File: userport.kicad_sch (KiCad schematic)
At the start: 13 parts, among them J17 C64_Tape_Port, J18 BA60BC0WT, J19 C64_User_Port, U16 74LVC374, U17 74LVC374, U18 74LS374, U19 74LS374, U20 74LS125, U21 74LS125, U23 74LVC374, U24 74LS125, U25 74LS374, U26 74LS374

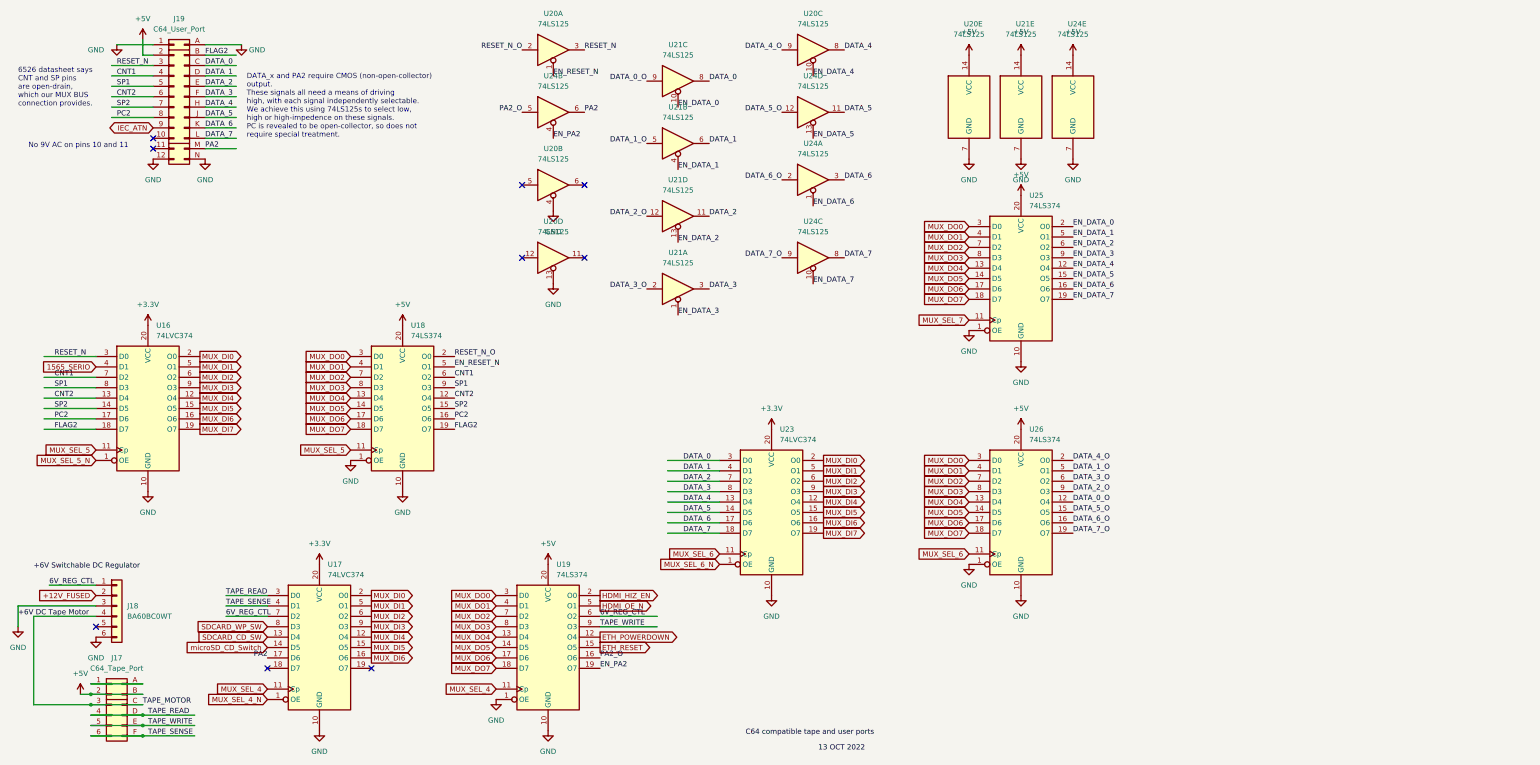
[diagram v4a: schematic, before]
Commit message: rework user port
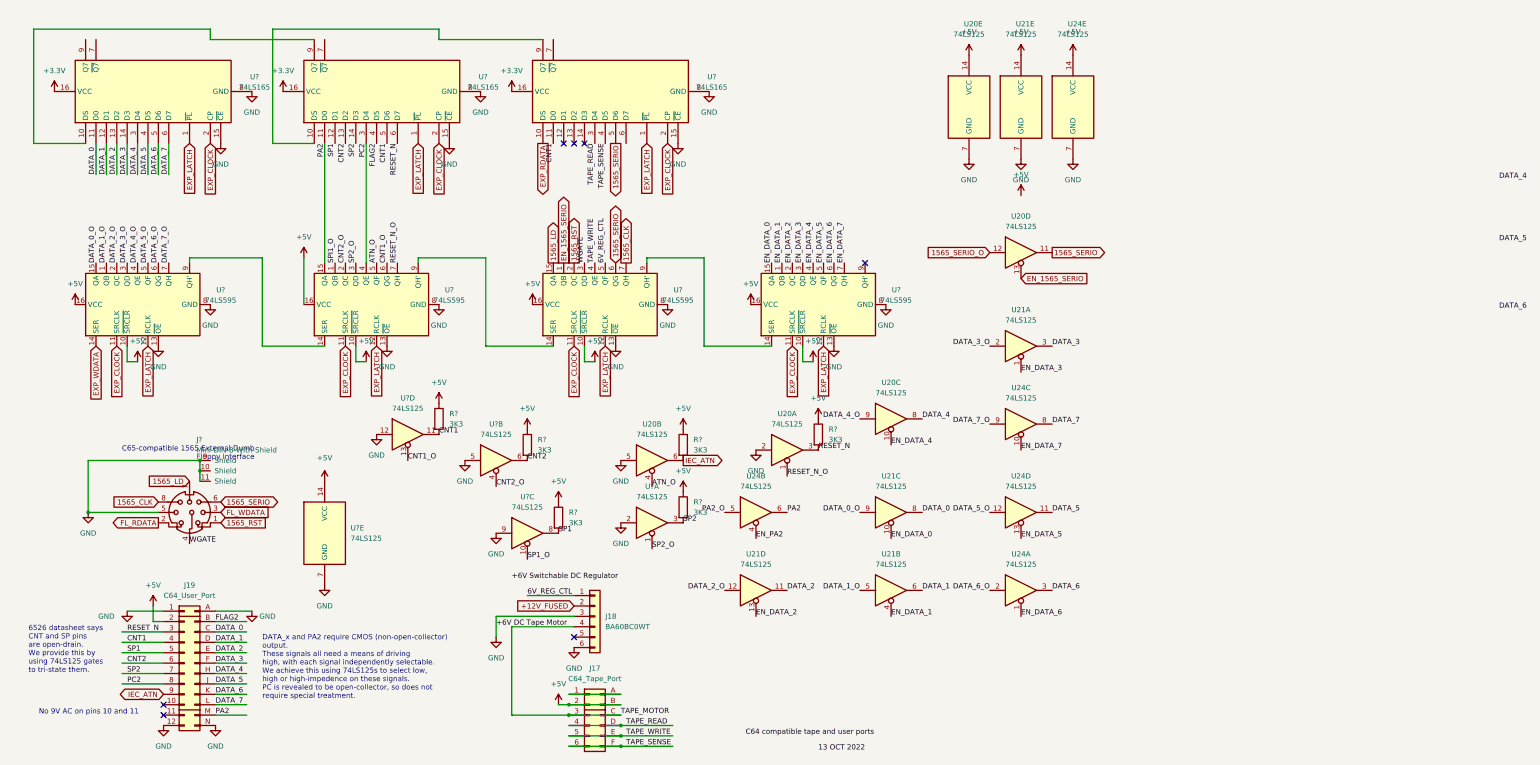
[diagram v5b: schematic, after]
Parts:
- removed U16, U17, U23: 74LVC374, snapeda:DIP-20_LVC_Family, symbol 74xx:74HC374
- removed U18, U19, U25, U26: 74LS374, snapeda:DIP-20_LS_Family, symbol 74xx:74LS374
- added J?: Mini-DIN-8-With-Shield, snapeda:mini-DIN-8, symbol 00Project-SDF-60J:Mini-DIN-8-With-Shield
- added R? (x6): 3K3, snapeda:Labeled Resistor, symbol Device:R
- added U? (x3): 74LS165, snapeda:DIP-16_LVC_Family, symbol 74xx:74LS165
- added U? (x5): 74LS125, symbol 74xx:74LS125
- added U? (x4): 74LS595, snapeda:DIP-16_LS_Family, symbol 74xx:74LS595
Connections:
- net EN_RESET_N is gone; now on net RESET_N_O: U20.1
- net +3V3: now also U?.16 (VCC), U?.16 (VCC), U?.16 (VCC)
- net +5V: now also R?.1, R?.1, R?.1, R?.1, R?.1, R?.1, U?.10 (~{SRCLR}), U?.10 (~{SRCLR}), U?.10 (~{SRCLR}), U?.10 (~{SRCLR}), U?.14 (VCC), U?.16 (VCC), U?.16 (VCC), U?.16 (VCC), U?.16 (VCC)
- net 1565_SERIO: now also U20.11, J?.6, U?.5 (D6), U?.6 (QG)
- net 6V_REG_CTL: now also U?.5 (QF)
- net CNT1: now also R?.2, U?.11, U?.11 (D0), U?.5 (D6)
- net CNT2: now also R?.2, U?.13 (D2), U?.6
- net DATA_0: now also U?.11 (D0)
- net DATA_0_O: now also U?.15 (QA)
- net DATA_1: now also U?.12 (D1)
- net DATA_1_O: now also U?.1 (QB)
- net DATA_2: now also U?.13 (D2)
- net DATA_2_O: now also U?.2 (QC)
- net DATA_3: now also U?.14 (D3)
- net DATA_3_O: now also U?.3 (QD)
- net DATA_4: now also U?.3 (D4)
- net DATA_4_O: now also U?.4 (QE)
- net DATA_5: now also U?.4 (D5)
- net DATA_5_O: now also U?.5 (QF)
- net DATA_6: now also U?.5 (D6)
- net DATA_6_O: now also U?.6 (QG)
- net DATA_7: now also U?.6 (D7)
- net DATA_7_O: now also U?.7 (QH)
- net EN_DATA_0: now also U?.15 (QA)
- net EN_DATA_1: now also U?.1 (QB)
- net EN_DATA_2: now also U?.2 (QC)
- net EN_DATA_3: now also U?.3 (QD)
- net EN_DATA_4: now also U?.4 (QE)
- net EN_DATA_5: now also U?.5 (QF)
- net EN_DATA_6: now also U?.6 (QG)
- net EN_DATA_7: now also U?.7 (QH)
- net FLAG2: now also U?.4 (D5)
- net GND: now also U20.2, U20.5, J?.10 (Shield), J?.11 (Shield), J?.5, J?.9 (Shield), U?.12, U?.13 (~{OE}), U?.13 (~{OE}), U?.13 (~{OE}), U?.13 (~{OE}), U?.15 (~{CE}), U?.15 (~{CE}), U?.15 (~{CE}), U?.2, U?.5, U?.7 (GND), U?.8 (GND), U?.8 (GND), U?.8 (GND), U?.8 (GND), U?.8 (GND), U?.8 (GND), U?.8 (GND), U?.9; no longer U20.13, U20.4
- net IEC_ATN: now also U20.6, R?.2
- net PA2: now also U?.11 (D0), U?.15 (QA)
- net PC2: now also U?.3 (D4), U?.4 (QE)
- net RESET_N: now also R?.2, U?.6 (D7)
- net RESET_N_O: now also U?.7 (QH); no longer U20.2
- net SP1: now also R?.2, U?.12 (D1), U?.8
- net SP2: now also R?.2, U?.14 (D3), U?.3
- net TAPE_READ: now also U?.3 (D4)
- net TAPE_SENSE: now also U?.4 (D5)
- net TAPE_WRITE: now also U?.4 (QE)
- net 1565_SERIO_O: now reaches U20.12
- new net: U?.10 (DS), U?.9 (Q7) (x2)
- new net: U?.14 (SER), U?.9 (QH') (x3)
- new net 1565_CLK: J?.8, U?.7 (QH)
- new net 1565_LD: J?.7, U?.15 (QA)
- new net 1565_RST: J?.1, U?.2 (QC)
- new net ATN_O: U20.4, U?.5 (QF)
- new net CNT1_O: U?.13, U?.6 (QG)
- new net CNT2_O: U?.2 (QC), U?.4
- new net EN_1565_SERIO: U20.13, U?.1 (QB)
- new net EXP_CLOCK: U?.11 (SRCLK), U?.11 (SRCLK), U?.11 (SRCLK), U?.11 (SRCLK), U?.2 (CP), U?.2 (CP), U?.2 (CP)
- new net EXP_LATCH: U?.1 (~{PL}), U?.1 (~{PL}), U?.1 (~{PL}), U?.12 (RCLK), U?.12 (RCLK), U?.12 (RCLK), U?.12 (RCLK)
- new net EXP_RDATA: U?.10 (DS)
- new net EXP_WDATA: U?.14 (SER)
- new net FL_RDATA: J?.2
- new net FL_WDATA: J?.3
- new net SP1_O: U?.10
- new net SP2_O: U?.1, U?.3 (QD)
- new net SPI1_O: U?.1 (QB)
- new net WGATE: J?.4, U?.3 (QD)
- no-connect marks 9 -> 7
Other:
- note added: "6526 datasheet says CNT and SP pins are open-drain. We provide this by using 74LS125 gates to tri-state them."
- note added: "C65-compatible 1565 External Dumb Floppy Interface"
- note removed: "6526 datasheet says CNT and SP pins are open-drain, which our MUX BUS connection provides."
- moved on the sheet: J17, J18, J19, U20A, U20B, U20C, U20D, U21A, U21B, U21C, U21D, U24A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

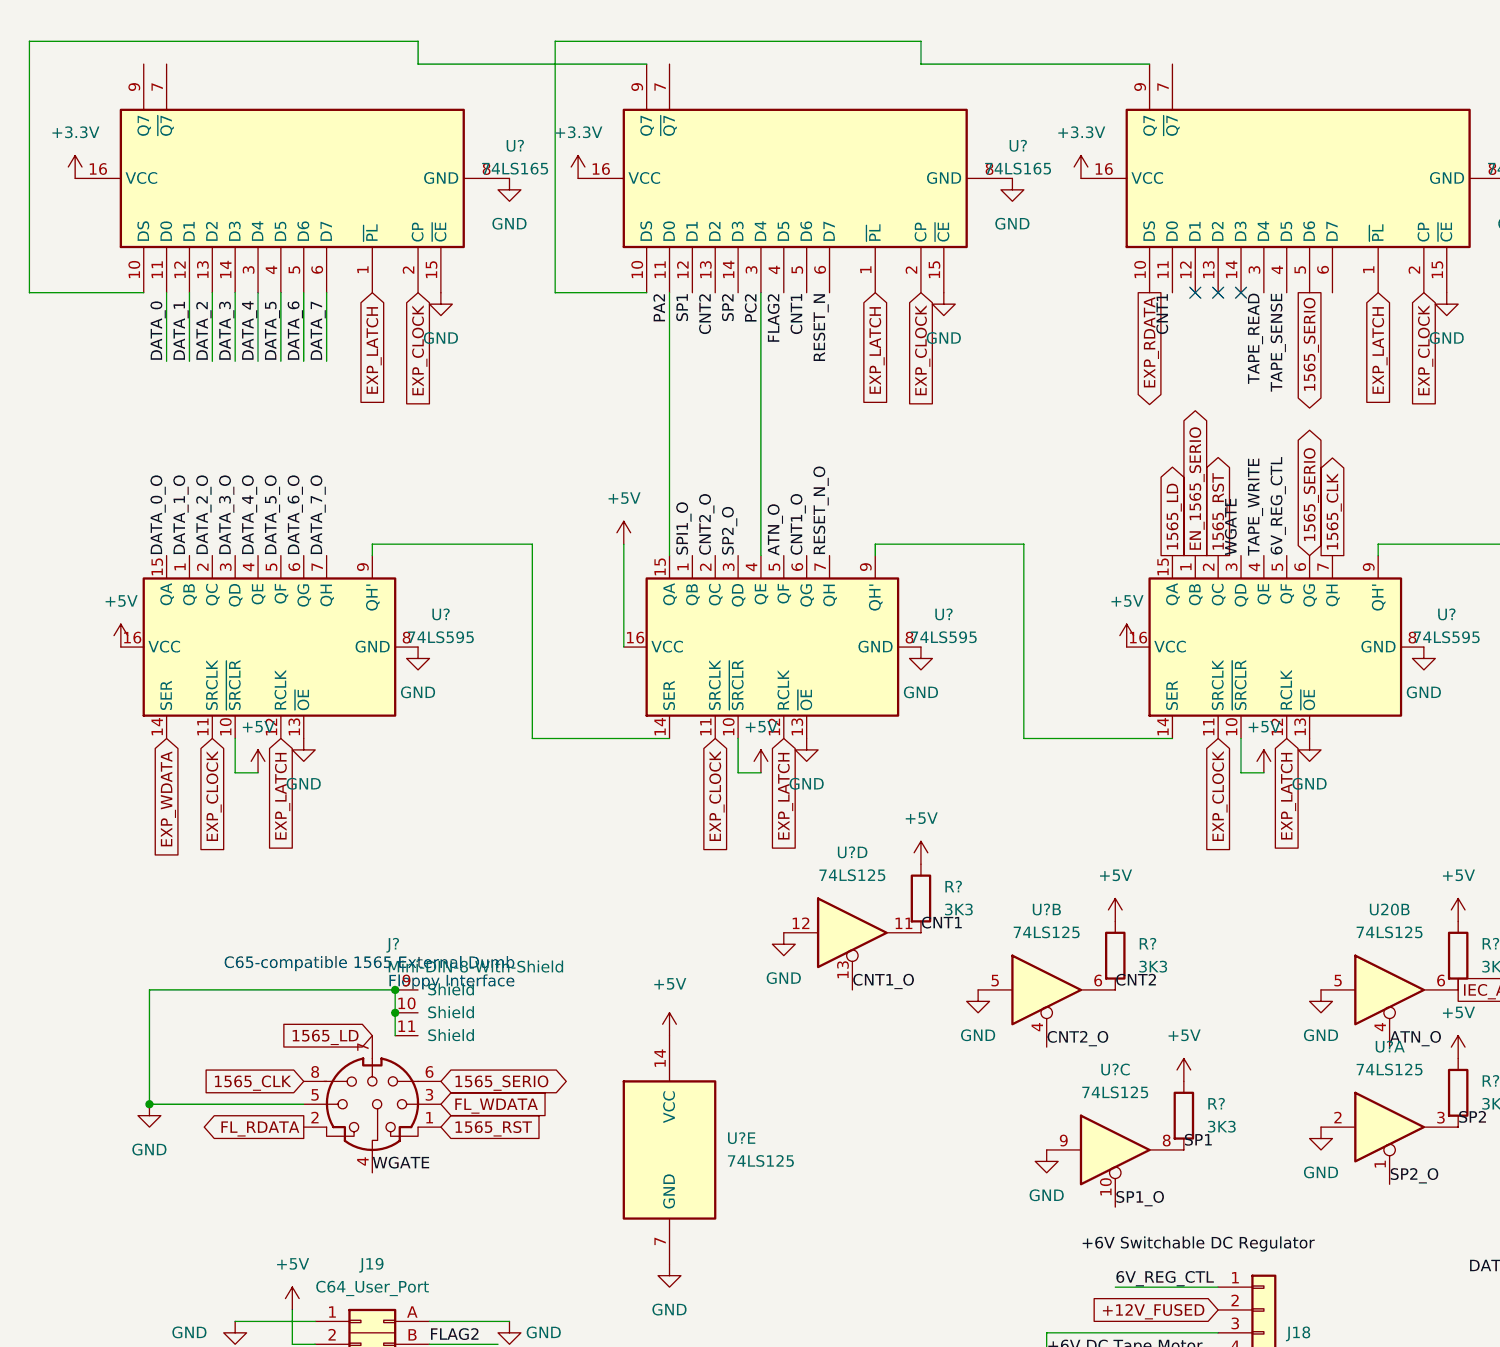
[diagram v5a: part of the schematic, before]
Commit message: reconnect everything and add PMOD and 34pin floppy connectors
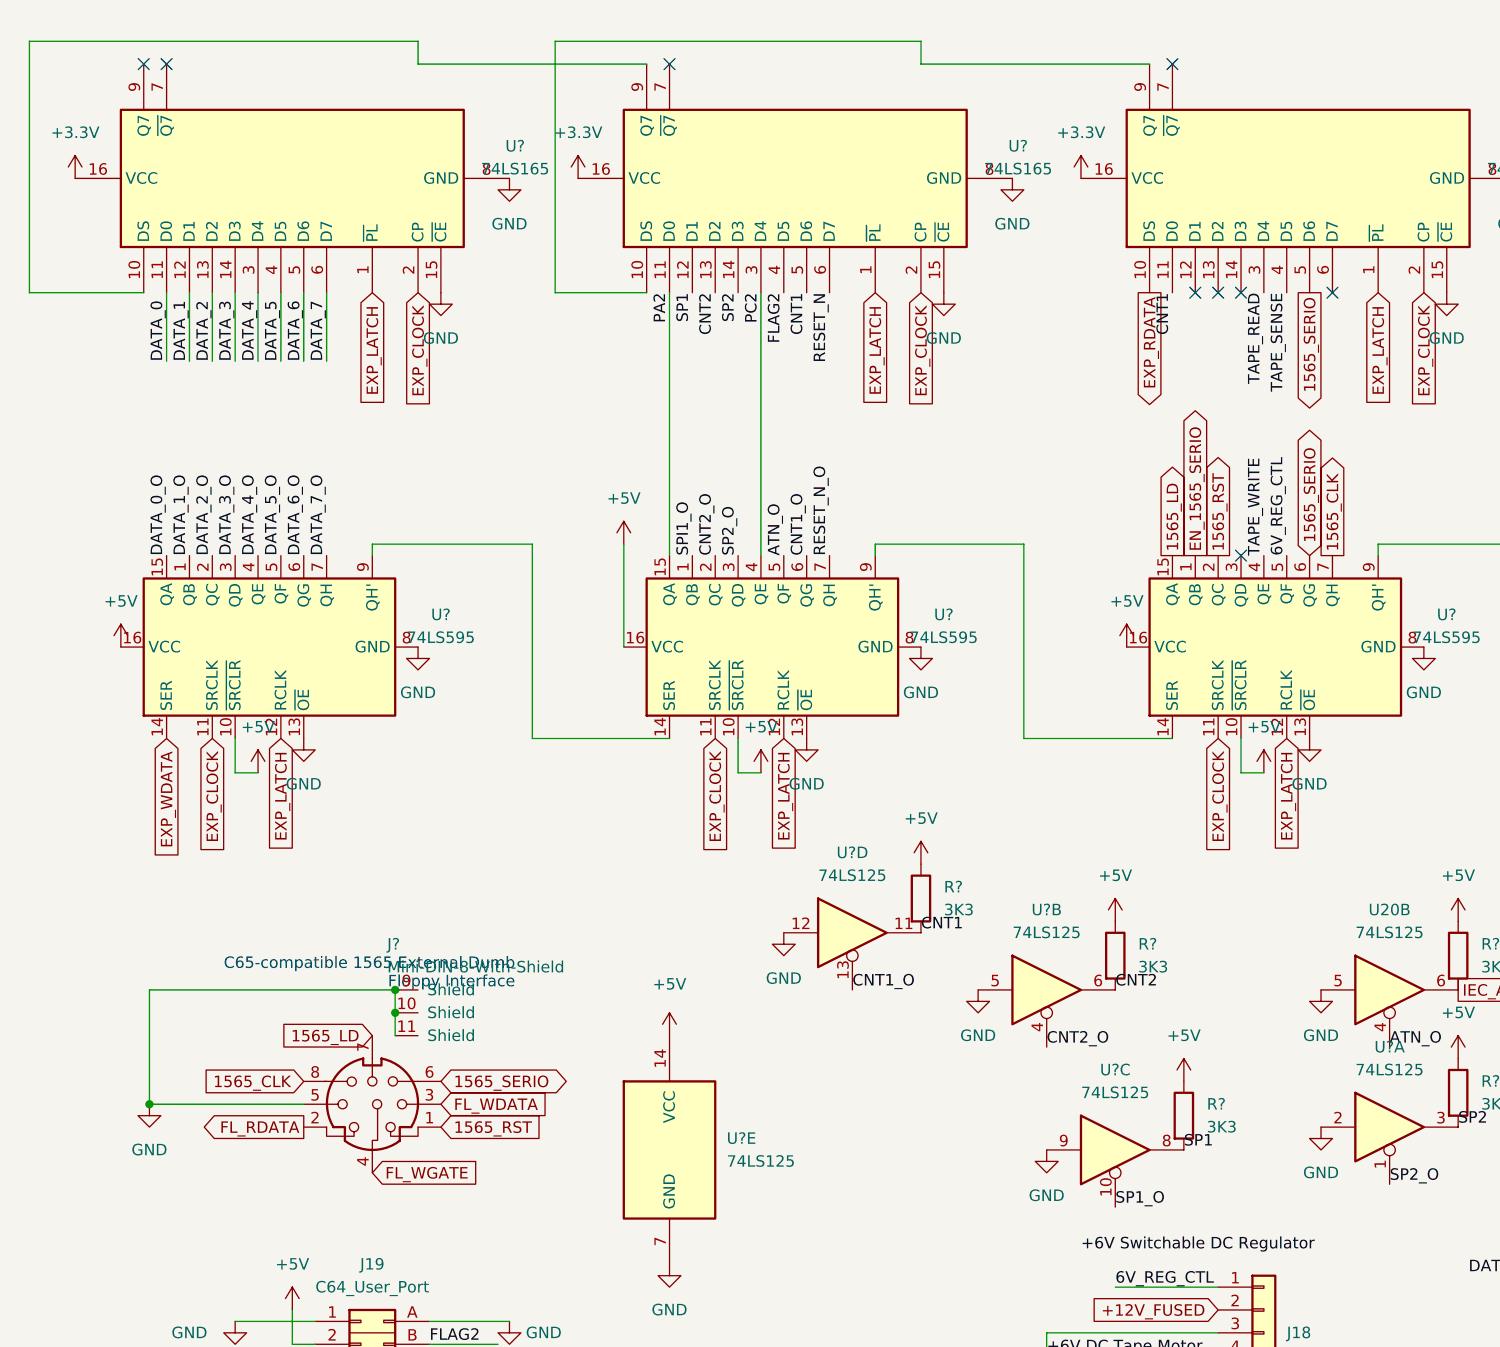
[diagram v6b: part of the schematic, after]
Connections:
- net WGATE: no longer names the net of U?.3 (QD)
- net WGATE: no longer J?.4
- new net FL_WGATE: J?.4
- no-connect marks 7 -> 13
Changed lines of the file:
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@@
   (junction (at 148.59 182.88) (diameter 0) (color 0 0 0 0)
   )
+  (no_connect (at 162.56 45.72))
+  (no_connect (at 88.9 20.32))
+  (no_connect (at 144.78 20.32))
+  (no_connect (at 30.48 20.32))
+  (no_connect (at 33.02 20.32))
   (no_connect (at 149.86 45.72))
   (no_connect (at 152.4 45.72))
   (no_connect (at 147.32 45.72))
+  (no_connect (at 152.4 74.93))
   (no_connect (at 49.53 182.88))
   (no_connect (at 149.86 166.37))
@@
     (effects (font (size 1.27 1.27)) (justify left bottom))
   )
-  (label "WGATE" (at 55.88 143.51 0)
-    (effects (font (size 1.27 1.27)) (justify left bottom))
-  )
   (label "DATA_0_O" (at 219.71 135.89 180)
     (effects (font (size 1.27 1.27)) (justify right bottom))
@@
   )
   (label "SP2" (at 176.53 138.43 0)
-    (effects (font (size 1.27 1.27)) (justify left bottom))
-  )
-  (label "WGATE" (at 152.4 74.93 90)
     (effects (font (size 1.27 1.27)) (justify left bottom))
   )
@@
     )
   )
+  (global_label "FL_WGATE" (shape input) (at 55.88 143.51 0) (fields_autoplaced)
+    (effects (font (size 1.27 1.27)) (justify left))
+    (property "Intersheet References" "${INTERSHEET_REFS}" (id 0) (at 67.2152 143.4306 0)
+      (effects (font (size 1.27 1.27)) (justify left) hide)
+    )
+  )

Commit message: begin placing and routing
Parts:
- gave numbers to parts that had none: 15

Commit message: yet more routing
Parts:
- U3: footprint (none) -> snapeda:DIP-14_74LS06
